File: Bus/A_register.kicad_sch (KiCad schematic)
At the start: 2 parts, among them J6 Conn_01x10_Pin, J7 Conn_01x04_Pin

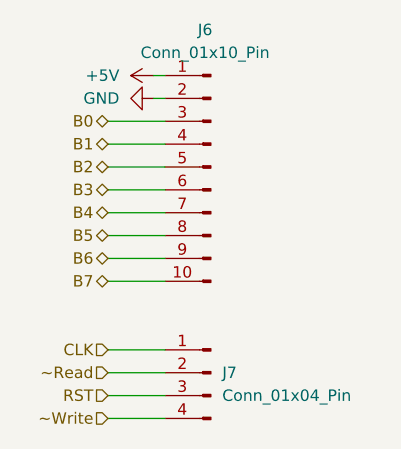
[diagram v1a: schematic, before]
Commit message: Updated bus schmatic pins to match final layouts
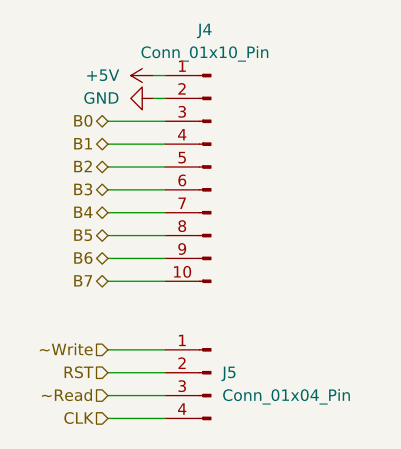
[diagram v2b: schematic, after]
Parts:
- renumbered J6 to J4, J7 to J5
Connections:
- net CLK: now also J5.4 (Pin_4); no longer J5.1 (Pin_1)
- net RST: now also J5.2 (Pin_2); no longer J5.3 (Pin_3)
- net ~Read: now also J5.3 (Pin_3); no longer J5.2 (Pin_2)
- net ~Write: now also J5.1 (Pin_1); no longer J5.4 (Pin_4)
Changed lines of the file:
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@@
 	(hierarchical_label "~Read"
 		(shape input)
-		(at 95.25 106.68 180)
+		(at 95.25 109.22 180)
 		(fields_autoplaced yes)
 		(effects
@@
 	(hierarchical_label "CLK"
 		(shape input)
-		(at 95.25 104.14 180)
+		(at 95.25 111.76 180)
 		(fields_autoplaced yes)
 		(effects
@@
 	(hierarchical_label "RST"
 		(shape input)
-		(at 95.25 109.22 180)
+		(at 95.25 106.68 180)
 		(fields_autoplaced yes)
 		(effects
@@
 	(hierarchical_label "~Write"
 		(shape input)
-		(at 95.25 111.76 180)
+		(at 95.25 104.14 180)
 		(fields_autoplaced yes)
 		(effects
@@
 		(on_board yes)
 		(dnp no)
-		(property "Reference" "J6"
+		(property "Reference" "J4"
 			(at 106.045 68.58 0)
 			(effects
@@
 		(instances
 			(project "bus"
-				(path "/37ae8b13-e183-404e-b70a-681e1af60f55/0ca11ce9-cbfc-4b57-961c-3886bedba2c0"
-					(reference "J6")
-					(unit 1)
-				)
 				(path "/37ae8b13-e183-404e-b70a-681e1af60f55/3ef390bf-8e1c-4d04-83d3-5133f3dd3ef5"
 					(reference "J4")
@@
 		(dnp no)
 		(fields_autoplaced yes)
-		(property "Reference" "#PWR09"
+		(property "Reference" "#PWR07"
 			(at 104.14 73.66 0)
 			(effects
@@
 		(instances
 			(project "bus"
-				(path "/37ae8b13-e183-404e-b70a-681e1af60f55/0ca11ce9-cbfc-4b57-961c-3886bedba2c0"
-					(reference "#PWR09")
-					(unit 1)
-				)
 				(path "/37ae8b13-e183-404e-b70a-681e1af60f55/3ef390bf-8e1c-4d04-83d3-5133f3dd3ef5"
 					(reference "#PWR07")
@@
 		(dnp no)
 		(fields_autoplaced yes)
-		(property "Reference" "J7"
+		(property "Reference" "J5"
 			(at 107.95 106.6799 0)
 			(effects
@@
 		(instances
 			(project "bus"
-				(path "/37ae8b13-e183-404e-b70a-681e1af60f55/0ca11ce9-cbfc-4b57-961c-3886bedba2c0"
-					(reference "J7")
-					(unit 1)
-				)
 				(path "/37ae8b13-e183-404e-b70a-681e1af60f55/3ef390bf-8e1c-4d04-83d3-5133f3dd3ef5"
 					(reference "J5")
@@
 		(dnp no)
 		(fields_autoplaced yes)
-		(property "Reference" "#PWR010"
+		(property "Reference" "#PWR08"
 			(at 93.98 76.2 0)
 			(effects
@@
 		(instances
 			(project "bus"
-				(path "/37ae8b13-e183-404e-b70a-681e1af60f55/0ca11ce9-cbfc-4b57-961c-3886bedba2c0"
-					(reference "#PWR010")
-					(unit 1)
-				)
 				(path "/37ae8b13-e183-404e-b70a-681e1af60f55/3ef390bf-8e1c-4d04-83d3-5133f3dd3ef5"
 					(reference "#PWR08")
